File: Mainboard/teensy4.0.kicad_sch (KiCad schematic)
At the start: 1 part, among them U1 Teensy4.0

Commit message: Mainboard grind
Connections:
- net BIAS_MOD_EN: now also U1.4 (2_OUT2)
- net LDAC_DAC: now also U1.9 (7_RX2_OUT1A); no longer U1.11 (9_OUT1C)
- net MISO_ADC: now reaches U1.14 (12_MISO_MQSL)
- net BUSY_ADC: now reaches U1.7 (5_IN2)
- net CNV_ADC: now reaches U1.8 (6_OUT1D)
- net SCK_DAC renamed SCK_ADC
- new net CS_ADC: U1.11 (9_OUT1C)
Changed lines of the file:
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@@
 	(generator_version "9.0")
 	(paper "A4")
+	(junction
+		(at 72.39 83.82)
+		(diameter 0)
+		(color 0 0 0 0)
+	)
 	(no_connect
 		(at 133.35 91.44)
@@
 	(wire
 		(pts
+			(xy 74.93 50.8) (xy 77.47 50.8)
+		)
+		(stroke
+			(width 0)
+			(type default)
+		)
+	)
+	(wire
+		(pts
+			(xy 74.93 55.88) (xy 77.47 55.88)
+		)
+		(stroke
+			(width 0)
+			(type default)
+		)
+	)
+	(wire
+		(pts
+			(xy 72.39 83.82) (xy 77.47 83.82)
+		)
+		(stroke
+			(width 0)
+			(type default)
+		)
+	)
+	(wire
+		(pts
 			(xy 133.35 96.52) (xy 140.97 96.52)
 		)
@@
 	(wire
 		(pts
+			(xy 74.93 53.34) (xy 77.47 53.34)
+		)
+		(stroke
+			(width 0)
+			(type default)
+		)
+	)
+	(wire
+		(pts
 			(xy 74.93 99.06) (xy 77.47 99.06)
 		)
@@
 	(wire
 		(pts
+			(xy 74.93 43.18) (xy 77.47 43.18)
+		)
+		(stroke
+			(width 0)
+			(type default)
+		)
+	)
+	(wire
+		(pts
+			(xy 72.39 83.82) (xy 72.39 86.36)
+		)
+		(stroke
+			(width 0)
+			(type default)
+		)
+	)
+	(wire
+		(pts
 			(xy 74.93 96.52) (xy 77.47 96.52)
 		)
@@
 	(wire
 		(pts
-			(xy 74.93 83.82) (xy 77.47 83.82)
+			(xy 71.12 86.36) (xy 72.39 86.36)
+		)
+		(stroke
+			(width 0)
+			(type default)
+		)
+	)
+	(wire
+		(pts
+			(xy 74.93 68.58) (xy 77.47 68.58)
+		)
+		(stroke
+			(width 0)
+			(type default)
+		)
+	)
+	(wire
+		(pts
+			(xy 71.12 83.82) (xy 72.39 83.82)
 		)
 		(stroke
@@
 		)
 	)
+	(hierarchical_label "BUSY_ADC"
+		(shape input)
+		(at 74.93 50.8 180)
+		(effects
+			(font
+				(size 1.27 1.27)
+			)
+			(justify right)
+		)
+	)
+	(hierarchical_label "LDAC_DAC"
+		(shape input)
+		(at 74.93 55.88 180)
+		(effects
+			(font
+				(size 1.27 1.27)
+			)
+			(justify right)
+		)
+	)
+	(hierarchical_label "SCK_ADC"
+		(shape input)
+		(at 71.12 86.36 180)
+		(effects
+			(font
+				(size 1.27 1.27)
+			)
+			(justify right)
+		)
+	)
 	(hierarchical_label "MOSI_DAC"
 		(shape input)
@@
 	(hierarchical_label "BIAS_MOD_EN"
 		(shape input)
-		(at 45.72 81.28 180)
+		(at 74.93 43.18 180)
+		(effects
+			(font
+				(size 1.27 1.27)
+			)
+			(justify right)
+		)
+	)
+	(hierarchical_label "CS_ADC"
+		(shape input)
+		(at 74.93 60.96 180)
 		(effects
 			(font
@@
 		)
 	)
-	(hierarchical_label "BIAS_MOD"
-		(shape input)
-		(at 45.72 76.2 180)
-		(effects
-			(font
-				(size 1.27 1.27)
-			)
-			(justify right)
-		)
-	)
 	(hierarchical_label "PS_Temp_SDA"
 		(shape input)
@@
 	(hierarchical_label "SCK_DAC"
 		(shape input)
-		(at 74.93 83.82 180)
+		(at 71.12 83.82 180)
+		(effects
+			(font
+				(size 1.27 1.27)
+			)
+			(justify right)
+		)
+	)
+	(hierarchical_label "CNV_ADC"
+		(shape input)
+		(at 74.93 53.34 180)
 		(effects
 			(font
@@
 		)
 	)
-	(hierarchical_label "LDAC_DAC"
-		(shape input)
-		(at 74.93 60.96 180)
-		(effects
-			(font
+	(hierarchical_label "MISO_ADC"
+		(shape input)
+		(at 74.93 68.58 180)
+		(effects
+			(font

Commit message: working mainboard push!
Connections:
- net BIAS_MOD_EN: now also U1.2 (0_RX1_CRX2_CS1); no longer U1.4 (2_OUT2)
- net GND: no longer U1.17 (GND), U1.32 (GND), U1.47 (GND)
- net DIR_1: now reaches U1.21 (14_A0_TX3_SPDIF_OUT)
- net STEP_1: now reaches U1.22 (15_A1_RX3_SPDIF_IN)
- net STEP_3: now reaches U1.3 (1_TX1_CTX2_MISO1)
- net STEP_2: now reaches U1.5 (3_LRCLK2)
- net DIR_2: now reaches U1.6 (4_BCLK2)
- new net DIR_3: U1.4 (2_OUT2)

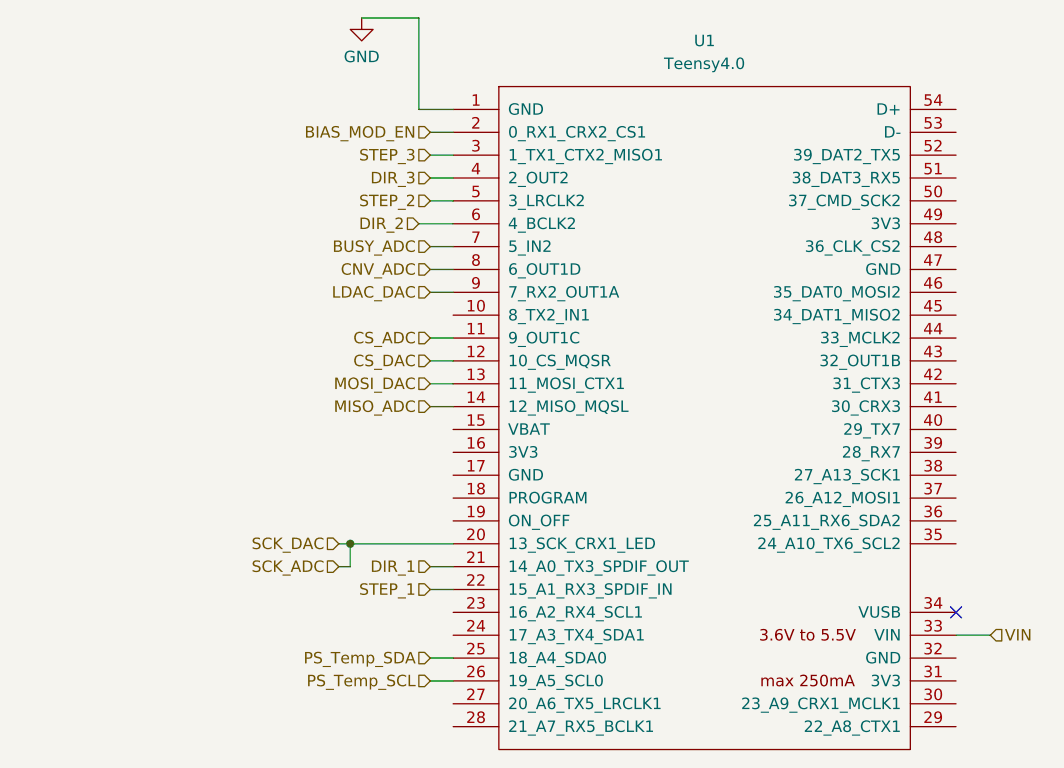
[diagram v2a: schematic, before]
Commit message: mainboard working commits!
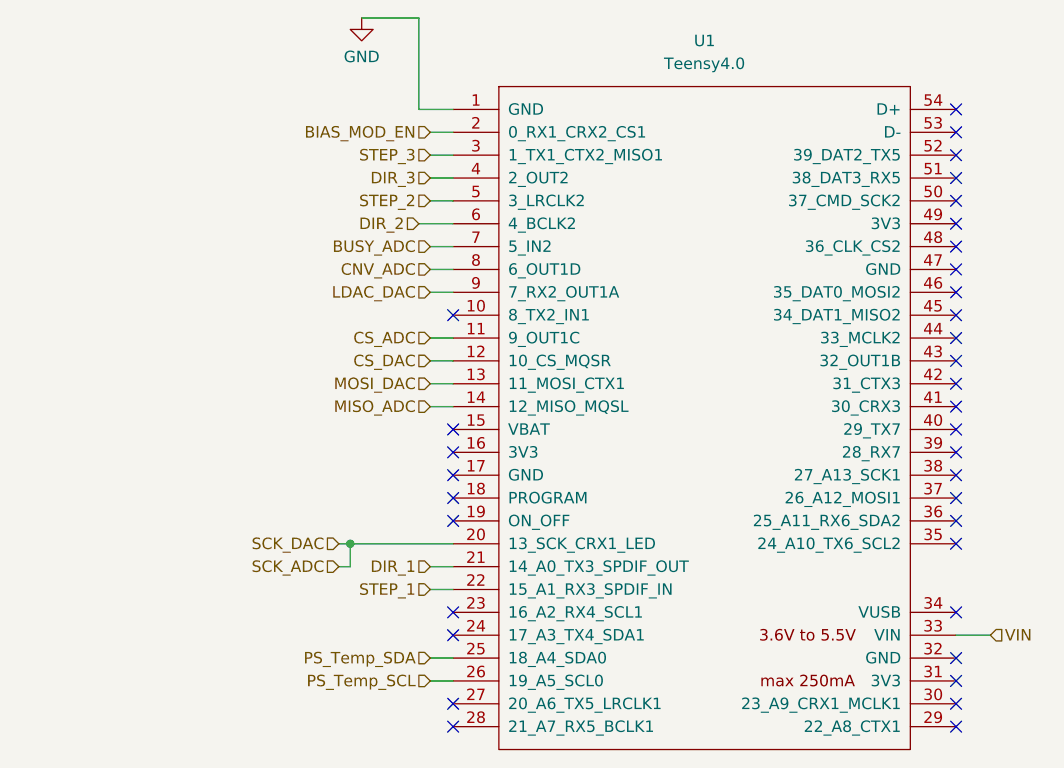
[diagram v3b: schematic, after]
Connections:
- no-connect marks 1 -> 35
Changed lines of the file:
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@@
+	)
+	(no_connect
+		(at 133.35 71.12)
+	)
+	(no_connect
+		(at 77.47 58.42)
+	)
+	(no_connect
+		(at 133.35 43.18)
+	)
+	(no_connect
+		(at 133.35 78.74)
+	)
+	(no_connect
+		(at 133.35 99.06)
+	)
+	(no_connect
+		(at 133.35 35.56)
+	)
+	(no_connect
+		(at 77.47 104.14)
+	)
+	(no_connect
+		(at 133.35 40.64)
 	)
 	(no_connect
 		(at 133.35 91.44)
 	)
+	(no_connect
+		(at 133.35 53.34)
+	)
+	(no_connect
+		(at 77.47 81.28)
+	)
+	(no_connect
+		(at 133.35 96.52)
+	)
+	(no_connect
+		(at 77.47 93.98)
+	)
+	(no_connect
+		(at 133.35 60.96)
+	)
+	(no_connect
+		(at 133.35 73.66)
+	)
+	(no_connect
+		(at 133.35 81.28)
+	)
+	(no_connect
+		(at 133.35 66.04)
+	)
+	(no_connect
+		(at 133.35 76.2)
+	)
+	(no_connect
+		(at 133.35 55.88)
+	)
+	(no_connect
+		(at 133.35 38.1)
+	)
+	(no_connect
+		(at 133.35 104.14)
+	)
+	(no_connect
+		(at 133.35 50.8)
+	)
+	(no_connect
+		(at 133.35 101.6)
+	)
+	(no_connect
+		(at 133.35 63.5)
+	)
+	(no_connect
+		(at 77.47 71.12)
+	)
+	(no_connect
+		(at 77.47 101.6)
+	)
+	(no_connect
+		(at 133.35 68.58)
+	)
+	(no_connect
+		(at 133.35 45.72)
+	)
+	(no_connect
+		(at 77.47 73.66)
+	)
+	(no_connect
+		(at 77.47 91.44)
+	)
+	(no_connect
+		(at 133.35 48.26)
+	)
+	(no_connect
+		(at 77.47 78.74)
+	)
+	(no_connect
+		(at 133.35 83.82)
+	)
+	(no_connect
+		(at 133.35 58.42)
+	)
+	(no_connect
+		(at 77.47 76.2)
+	)
 	(wire
